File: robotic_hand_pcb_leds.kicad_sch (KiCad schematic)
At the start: 5 parts, among them J4 WS2812B

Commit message: Pass ERC
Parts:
- removed J4: WS2812B, symbol Connector:Conn_01x03_Pin
- added J14: WS2812B, symbol Connector:Conn_01x03_Pin
- added J15: Photodiode, symbol Connector:Conn_01x01_Pin
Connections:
- net +5V: now also J14.2 (Pin_2)
- net GND: now also J14.3 (Pin_3)
- net at D4.2 (DOUT): now also J14.1 (Pin_1)
- new net ADC_PHOTODIODE: J15.1 (Pin_1)
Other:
- note added: "WIP - Photodiode"

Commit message: Update for WIP changes
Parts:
- removed J15: Photodiode, symbol Connector:Conn_01x01_Pin
- renumbered J14 to J6
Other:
- note removed: "WIP - Photodiode"
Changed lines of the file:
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@@
-	(wire
-		(pts
-			(xy 38.1 76.2) (xy 63.5 76.2)
-		)
-		(stroke
-			(width 0)
-			(type default)
-		)
-	)
 	(wire
 		(pts
@@
 		)
 	)
-	(text "WIP - Photodiode"
-		(exclude_from_sim no)
-		(at 63.246 84.582 0)
-		(effects
-			(font
-				(size 3.175 3.175)
-				(thickness 0.635)
-				(bold yes)
-				(italic yes)
-			)
-		)
-	)
-	(hierarchical_label "ADC_PHOTODIODE"
-		(shape input)
-		(at 38.1 76.2 180)
-		(effects
-			(font
-				(size 1.27 1.27)
-			)
-			(justify right)
-		)
-	)
 	(hierarchical_label "WS2812B_PWM"
 		(shape input)
@@
 		(dnp no)
 		(fields_autoplaced yes)
-		(property "Reference" "#PWR062"
+		(property "Reference" "#PWR056"
 			(at 107.95 54.61 0)
 			(effects
@@
 			(project "robotic_hand_pcb"
 				(path "/96df9010-a1f8-4419-aac0-9388de87cb21/778b6ab7-1162-4b51-a46c-fb76fabecb49"
-					(reference "#PWR062")
+					(reference "#PWR056")
 					(unit 1)
 				)
@@
 		(dnp no)
 		(fields_autoplaced yes)
-		(property "Reference" "J14"
+		(property "Reference" "J6"
 			(at 133.35 40.6399 0)
 			(effects
@@
 			(project "robotic_hand_pcb"
 				(path "/96df9010-a1f8-4419-aac0-9388de87cb21/778b6ab7-1162-4b51-a46c-fb76fabecb49"
-					(reference "J14")
+					(reference "J6")
 					(unit 1)
 				)
@@
 		(dnp no)
 		(fields_autoplaced yes)
-		(property "Reference" "#PWR058"
+		(property "Reference" "#PWR052"
 			(at 125.73 52.07 0)
 			(effects
@@
 			(project "robotic_hand_pcb"
 				(path "/96df9010-a1f8-4419-aac0-9388de87cb21/778b6ab7-1162-4b51-a46c-fb76fabecb49"
-					(reference "#PWR058")
+					(reference "#PWR052")
 					(unit 1)
 				)
@@
 		(on_board yes)
 		(dnp no)
-		(property "Reference" "#PWR056"
+		(property "Reference" "#PWR050"
 			(at 107.95 34.29 0)
 			(effects
@@
 			(project "robotic_hand_pcb"
 				(path "/96df9010-a1f8-4419-aac0-9388de87cb21/778b6ab7-1162-4b51-a46c-fb76fabecb49"
-					(reference "#PWR056")
+					(reference "#PWR050")
 					(unit 1)
 				)
@@
 		(dnp no)
 		(fields_autoplaced yes)
-		(property "Reference" "#PWR059"
+		(property "Reference" "#PWR053"
 			(at 50.8 54.61 0)
 			(effects
@@
 			(project "robotic_hand_pcb"
 				(path "/96df9010-a1f8-4419-aac0-9388de87cb21/778b6ab7-1162-4b51-a46c-fb76fabecb49"
-					(reference "#PWR059")
+					(reference "#PWR053")
 					(unit 1)
 				)
@@
 		(on_board yes)
 		(dnp no)
-		(property "Reference" "#PWR053"
+		(property "Reference" "#PWR047"
 			(at 50.8 34.29 0)
 			(effects
@@
 			(project "robotic_hand_pcb"
 				(path "/96df9010-a1f8-4419-aac0-9388de87cb21/778b6ab7-1162-4b51-a46c-fb76fabecb49"
-					(reference "#PWR053")
+					(reference "#PWR047")
 					(unit 1)
 				)
@@
 		(on_board yes)
 		(dnp no)
-		(property "Reference" "#PWR055"
+		(property "Reference" "#PWR049"
 			(at 88.9 34.29 0)
 			(effects
@@
 			(project "robotic_hand_pcb"
 				(path "/96df9010-a1f8-4419-aac0-9388de87cb21/778b6ab7-1162-4b51-a46c-fb76fabecb49"
-					(reference "#PWR055")
-					(unit 1)
-				)
-			)
-		)
-	)
-	(symbol
-		(lib_id "Connector:Conn_01x01_Pin")
-		(at 68.58 76.2 0)
-		(mirror y)
-		(unit 1)
-		(exclude_from_sim no)
-		(in_bom yes)
-		(on_board yes)
-		(dnp no)
-		(property "Reference" "J15"
-			(at 69.85 74.93 0)
-			(effects
-				(font
-					(size 1.27 1.27)
-				)
-				(justify right)
-			)
-		)
-		(property "Value" "Photodiode"
-			(at 69.85 77.47 0)
-			(effects
-				(font
-					(size 1.27 1.27)
-				)
-				(justify right)
-			)
-		)
-		(property "Footprint" ""
-			(at 68.58 76.2 0)
-			(effects
-				(font
-					(size 1.27 1.27)
-				)
-				(hide yes)
-			)
-		)
-		(property "Datasheet" "~"
-			(at 68.58 76.2 0)
-			(effects
-				(font
-					(size 1.27 1.27)
-				)
-				(hide yes)
-			)
-		)
-		(property "Description" "Generic connector, single row, 01x01, script generated"
-			(at 68.58 76.2 0)
-			(effects
-				(font
-					(size 1.27 1.27)
-				)
-				(hide yes)
-			)
-		)
-		(pin "1"
-		)
-		(instances
-			(project ""
-				(path "/96df9010-a1f8-4419-aac0-9388de87cb21/778b6ab7-1162-4b51-a46c-fb76fabecb49"
-					(reference "J15")
+					(reference "#PWR049")
 					(unit 1)
 				)
@@
 		(dnp no)
 		(fields_autoplaced yes)
-		(property "Reference" "#PWR061"
+		(property "Reference" "#PWR055"
 			(at 88.9 54.61 0)
 			(effects
@@
 			(project "robotic_hand_pcb"
 				(path "/96df9010-a1f8-4419-aac0-9388de87cb21/778b6ab7-1162-4b51-a46c-fb76fabecb49"
-					(reference "#PWR061")
+					(reference "#PWR055")
 					(unit 1)
 				)
@@
 		(on_board yes)
 		(dnp no)
-		(property "Reference" "#PWR054"
+		(property "Reference" "#PWR048"
 			(at 69.85 34.29 0)
 			(effects
@@
 			(project "robotic_hand_pcb"
 				(path "/96df9010-a1f8-4419-aac0-9388de87cb21/778b6ab7-1162-4b51-a46c-fb76fabecb49"
-					(reference "#PWR054")
+					(reference "#PWR048")
 					(unit 1)
 				)
@@
 		(on_board yes)
 		(dnp no)
-		(property "Reference" "#PWR057"
+		(property "Reference" "#PWR051"
 			(at 124.46 34.29 0)
 			(effects
@@
 			(project "robotic_hand_pcb"
 				(path "/96df9010-a1f8-4419-aac0-9388de87cb21/778b6ab7-1162-4b51-a46c-fb76fabecb49"
-					(reference "#PWR057")
+					(reference "#PWR051")
 					(unit 1)
 				)
@@
 		(dnp no)
 		(fields_autoplaced yes)
-		(property "Reference" "#PWR060"
+		(property "Reference" "#PWR054"
 			(at 69.85 54.61 0)
 			(effects
@@
 			(project "robotic_hand_pcb"
 				(path "/96df9010-a1f8-4419-aac0-9388de87cb21/778b6ab7-1162-4b51-a46c-fb76fabecb49"
-					(reference "#PWR060")
-					(unit 1)
-				)
+					(reference "#PWR054")
+					(unit 1)
+				)

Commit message: Add WIP schematic changes
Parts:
- renumbered J6 to J5
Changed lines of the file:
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@@
 		(dnp no)
 		(fields_autoplaced yes)
-		(property "Reference" "#PWR056"
+		(property "Reference" "#PWR060"
 			(at 107.95 54.61 0)
 			(effects
@@
 			(project "robotic_hand_pcb"
 				(path "/96df9010-a1f8-4419-aac0-9388de87cb21/778b6ab7-1162-4b51-a46c-fb76fabecb49"
-					(reference "#PWR056")
+					(reference "#PWR060")
 					(unit 1)
 				)
@@
 		(dnp no)
 		(fields_autoplaced yes)
-		(property "Reference" "J6"
+		(property "Reference" "J5"
 			(at 133.35 40.6399 0)
 			(effects
@@
 			(project "robotic_hand_pcb"
 				(path "/96df9010-a1f8-4419-aac0-9388de87cb21/778b6ab7-1162-4b51-a46c-fb76fabecb49"
-					(reference "J6")
+					(reference "J5")
 					(unit 1)
 				)
@@
 		(dnp no)
 		(fields_autoplaced yes)
-		(property "Reference" "#PWR052"
+		(property "Reference" "#PWR056"
 			(at 125.73 52.07 0)
 			(effects
@@
 			(project "robotic_hand_pcb"
 				(path "/96df9010-a1f8-4419-aac0-9388de87cb21/778b6ab7-1162-4b51-a46c-fb76fabecb49"
-					(reference "#PWR052")
+					(reference "#PWR056")
 					(unit 1)
 				)
@@
 		(on_board yes)
 		(dnp no)
-		(property "Reference" "#PWR050"
+		(property "Reference" "#PWR054"
 			(at 107.95 34.29 0)
 			(effects
@@
 			(project "robotic_hand_pcb"
 				(path "/96df9010-a1f8-4419-aac0-9388de87cb21/778b6ab7-1162-4b51-a46c-fb76fabecb49"
-					(reference "#PWR050")
+					(reference "#PWR054")
 					(unit 1)
 				)
@@
 		(dnp no)
 		(fields_autoplaced yes)
-		(property "Reference" "#PWR053"
+		(property "Reference" "#PWR057"
 			(at 50.8 54.61 0)
 			(effects
@@
 			(project "robotic_hand_pcb"
 				(path "/96df9010-a1f8-4419-aac0-9388de87cb21/778b6ab7-1162-4b51-a46c-fb76fabecb49"
-					(reference "#PWR053")
+					(reference "#PWR057")
 					(unit 1)
 				)
@@
 		(on_board yes)
 		(dnp no)
-		(property "Reference" "#PWR047"
+		(property "Reference" "#PWR051"
 			(at 50.8 34.29 0)
 			(effects
@@
 			(project "robotic_hand_pcb"
 				(path "/96df9010-a1f8-4419-aac0-9388de87cb21/778b6ab7-1162-4b51-a46c-fb76fabecb49"
-					(reference "#PWR047")
+					(reference "#PWR051")
 					(unit 1)
 				)
@@
 		(on_board yes)
 		(dnp no)
-		(property "Reference" "#PWR049"
+		(property "Reference" "#PWR053"
 			(at 88.9 34.29 0)
 			(effects
@@
 			(project "robotic_hand_pcb"
 				(path "/96df9010-a1f8-4419-aac0-9388de87cb21/778b6ab7-1162-4b51-a46c-fb76fabecb49"
-					(reference "#PWR049")
+					(reference "#PWR053")
 					(unit 1)
 				)
@@
 		(dnp no)
 		(fields_autoplaced yes)
-		(property "Reference" "#PWR055"
+		(property "Reference" "#PWR059"
 			(at 88.9 54.61 0)
 			(effects
@@
 			(project "robotic_hand_pcb"
 				(path "/96df9010-a1f8-4419-aac0-9388de87cb21/778b6ab7-1162-4b51-a46c-fb76fabecb49"
-					(reference "#PWR055")
+					(reference "#PWR059")
 					(unit 1)
 				)
@@
 		(on_board yes)
 		(dnp no)
-		(property "Reference" "#PWR048"
+		(property "Reference" "#PWR052"
 			(at 69.85 34.29 0)
 			(effects
@@
 			(project "robotic_hand_pcb"
 				(path "/96df9010-a1f8-4419-aac0-9388de87cb21/778b6ab7-1162-4b51-a46c-fb76fabecb49"
-					(reference "#PWR048")
+					(reference "#PWR052")
 					(unit 1)
 				)
@@
 		(on_board yes)
 		(dnp no)
-		(property "Reference" "#PWR051"
+		(property "Reference" "#PWR055"
 			(at 124.46 34.29 0)
 			(effects
@@
 			(project "robotic_hand_pcb"
 				(path "/96df9010-a1f8-4419-aac0-9388de87cb21/778b6ab7-1162-4b51-a46c-fb76fabecb49"
-					(reference "#PWR051")
+					(reference "#PWR055")
 					(unit 1)
 				)
@@
 		(dnp no)
 		(fields_autoplaced yes)
-		(property "Reference" "#PWR054"
+		(property "Reference" "#PWR058"
 			(at 69.85 54.61 0)
 			(effects
@@
 			(project "robotic_hand_pcb"
 				(path "/96df9010-a1f8-4419-aac0-9388de87cb21/778b6ab7-1162-4b51-a46c-fb76fabecb49"
-					(reference "#PWR054")
-					(unit 1)
-				)
+					(reference "#PWR058")
+					(unit 1)
+				)

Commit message: Assign footprints
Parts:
- J5: footprint (none) -> Connector_PinHeader_2.54mm:PinHeader_1x03_P2.54mm_Vertical
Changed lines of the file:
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@@
 			)
 		)
-		(property "Footprint" ""
+		(property "Footprint" "Connector_PinHeader_2.54mm:PinHeader_1x03_P2.54mm_Vertical"
 			(at 132.08 41.91 0)
 			(effects

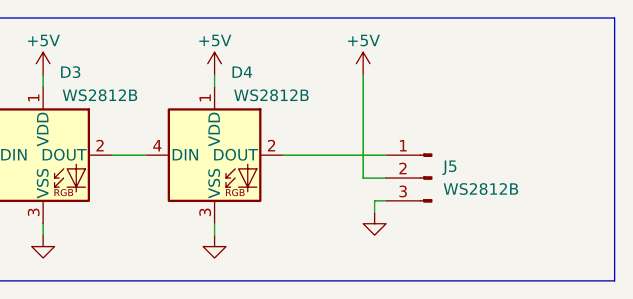
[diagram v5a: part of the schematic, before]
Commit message: Add WIP PCB layout and routing
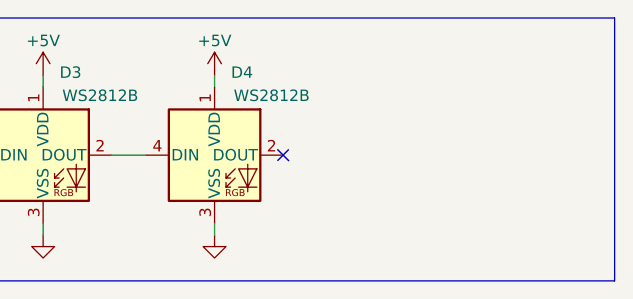
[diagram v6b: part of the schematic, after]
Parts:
- removed J5: WS2812B, Connector_PinHeader_2.54mm:PinHeader_1x03_P2.54mm_Vertical, symbol Connector:Conn_01x03_Pin
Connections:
- no-connect marks 0 -> 1

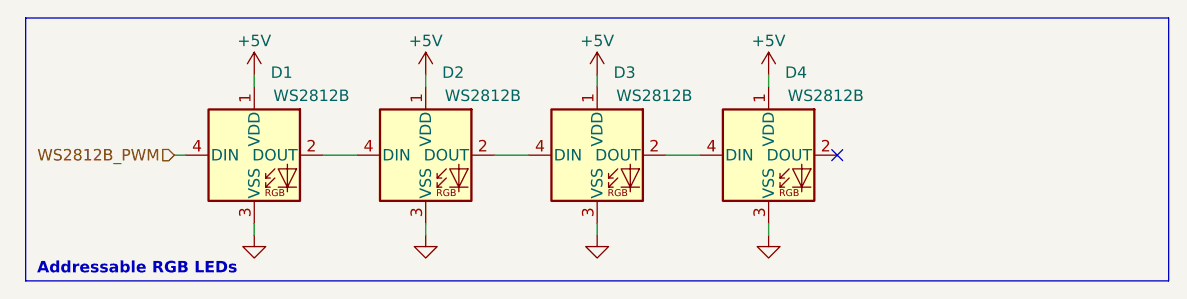
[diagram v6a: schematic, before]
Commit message: Update WIP, clean up stepper drivers
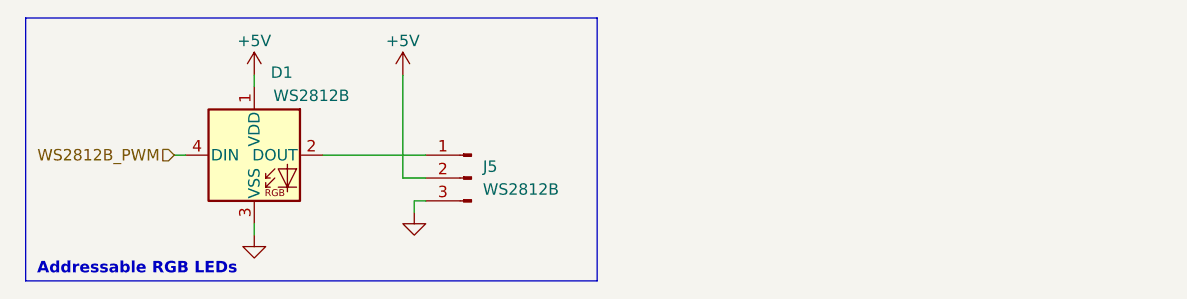
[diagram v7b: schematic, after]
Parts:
- removed D2, D3, D4: WS2812B, LED_SMD:LED_WS2812B_PLCC4_5.0x5.0mm_P3.2mm, symbol LED:WS2812B
- added J5: WS2812B, Connector_PinHeader_2.54mm:PinHeader_1x03_P2.54mm_Vertical, symbol Connector:Conn_01x03_Pin
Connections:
- net +5V: now also J5.2 (Pin_2)
- net GND: now also J5.3 (Pin_3)
- net at D1.2 (DOUT): now also J5.1 (Pin_1)
- no-connect marks 1 -> 0
